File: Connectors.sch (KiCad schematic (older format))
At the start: 6 parts, among them J201 Conn_ARM_JTAG_SWD_10, J202 Conn_01x10, J203 Conn_01x04, J204 Conn_02x03_Counter_Clockwise

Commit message: updates to schematic
Signed-off-by: Thomas Schmid <tom@binary-kitchen.de>
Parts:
- J201: renamed from J202; footprint Connector_Molex:Molex_Micro-Latch_53254-1070_1x10_P2.00mm_Horizontal -> Connector_Molex:Molex_MicroClasp_55935-1010_1x10_P2.00mm_Horizontal
- J202: renamed from J201; footprint Connector_PinHeader_2.54mm:PinHeader_2x05_P2.54mm_Vertical -> Connector_PinHeader_2.00mm:PinHeader_2x05_P2.00mm_Vertical_SMD
- J203: renamed from J204; footprint Connector_PinHeader_2.54mm:PinHeader_2x03_P2.54mm_Horizontal -> Connector_PinHeader_2.00mm:PinHeader_2x05_P2.00mm_Vertical_SMD
- renumbered J203 to J204
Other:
- note added: "mosfets: Si7232DN"
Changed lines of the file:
@@
 $EndDescr
 $Comp
-L Connector:Conn_ARM_JTAG_SWD_10 J201
+L Connector:Conn_ARM_JTAG_SWD_10 J202
 U 1 1 5D3DE887
 P 2000 1500
-F 0 "J201" H 1557 1546 50  0000 R CNN
+F 0 "J202" H 1557 1546 50  0000 R CNN
 F 1 "Conn_ARM_JTAG_SWD_10" H 1557 1455 50  0000 R CNN
-F 2 "Connector_PinHeader_2.54mm:PinHeader_2x05_P2.54mm_Vertical" H 2000 1500 50  0001 C CNN
+F 2 "Connector_PinHeader_2.00mm:PinHeader_2x05_P2.00mm_Vertical_SMD" H 2000 1500 50  0001 C CNN
 F 3 "http://infocenter.arm.com/help/topic/com.arm.doc.ddi0314h/DDI0314H_coresight_components_trm.pdf" V 1650 250 50  0001 C CNN
 	1    2000 1500
@@
 ARM_L
 $Comp
-L Connector_Generic:Conn_01x10 J202
+L Connector_Generic:Conn_01x10 J201
 U 1 1 5D607587
 P 1600 3250
-F 0 "J202" H 1680 3242 50  0000 L CNN
+F 0 "J201" H 1680 3242 50  0000 L CNN
 F 1 "Conn_01x10" H 1680 3151 50  0000 L CNN
-F 2 "Connector_Molex:Molex_Micro-Latch_53254-1070_1x10_P2.00mm_Horizontal" H 1600 3250 50  0001 C CNN
+F 2 "Connector_Molex:Molex_MicroClasp_55935-1010_1x10_P2.00mm_Horizontal" H 1600 3250 50  0001 C CNN
 F 3 "~" H 1600 3250 50  0001 C CNN
 	1    1600 3250
@@
 $EndComp
 $Comp
-L Connector_Generic:Conn_01x04 J203
+L Connector_Generic:Conn_01x04 J204
 U 1 1 5D616D6A
 P 3250 2750
-F 0 "J203" H 3330 2742 50  0000 L CNN
+F 0 "J204" H 3330 2742 50  0000 L CNN
 F 1 "Conn_01x04" H 3330 2651 50  0000 L CNN
 F 2 "Connector_Molex:Molex_PicoBlade_53048-0410_1x04_P1.25mm_Horizontal" H 3250 2750 50  0001 C CNN
@@
 $EndComp
 $Comp
-L Connector_Generic:Conn_02x03_Counter_Clockwise J204
+L Connector_Generic:Conn_02x03_Counter_Clockwise J203
 U 1 1 5D61EC32
 P 3200 3500
-F 0 "J204" H 3250 3817 50  0000 C CNN
+F 0 "J203" H 3250 3817 50  0000 C CNN
 F 1 "Conn_02x03_Counter_Clockwise" H 3250 3726 50  0000 C CNN
-F 2 "Connector_PinHeader_2.54mm:PinHeader_2x03_P2.54mm_Horizontal" H 3200 3500 50  0001 C CNN
+F 2 "Connector_PinHeader_2.00mm:PinHeader_2x05_P2.00mm_Vertical_SMD" H 3200 3500 50  0001 C CNN
 F 3 "~" H 3200 3500 50  0001 C CNN
 	1    3200 3500
@@
 	1    0    0    -1
 $EndComp
+Text Notes 3100 1200 0    50   ~ 0
+mosfets: Si7232DN
 $EndSCHEMATC

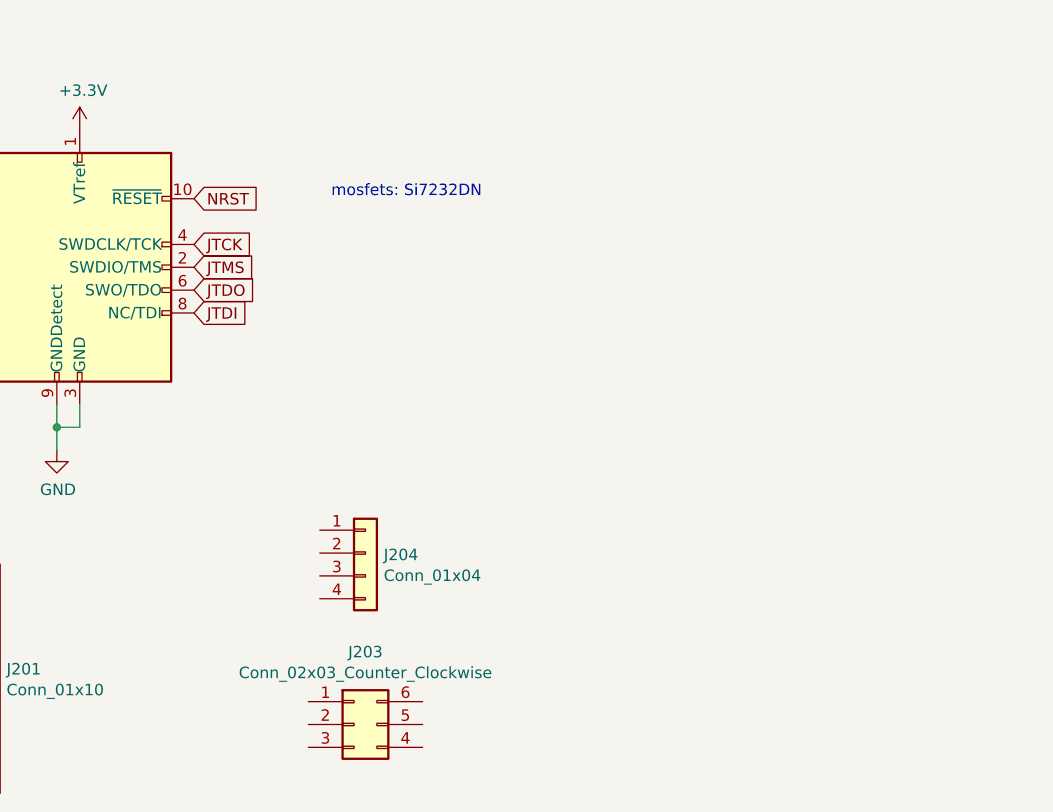
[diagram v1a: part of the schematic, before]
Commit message: add pyro output stages
Signed-off-by: Thomas Schmid <tom@binary-kitchen.de>
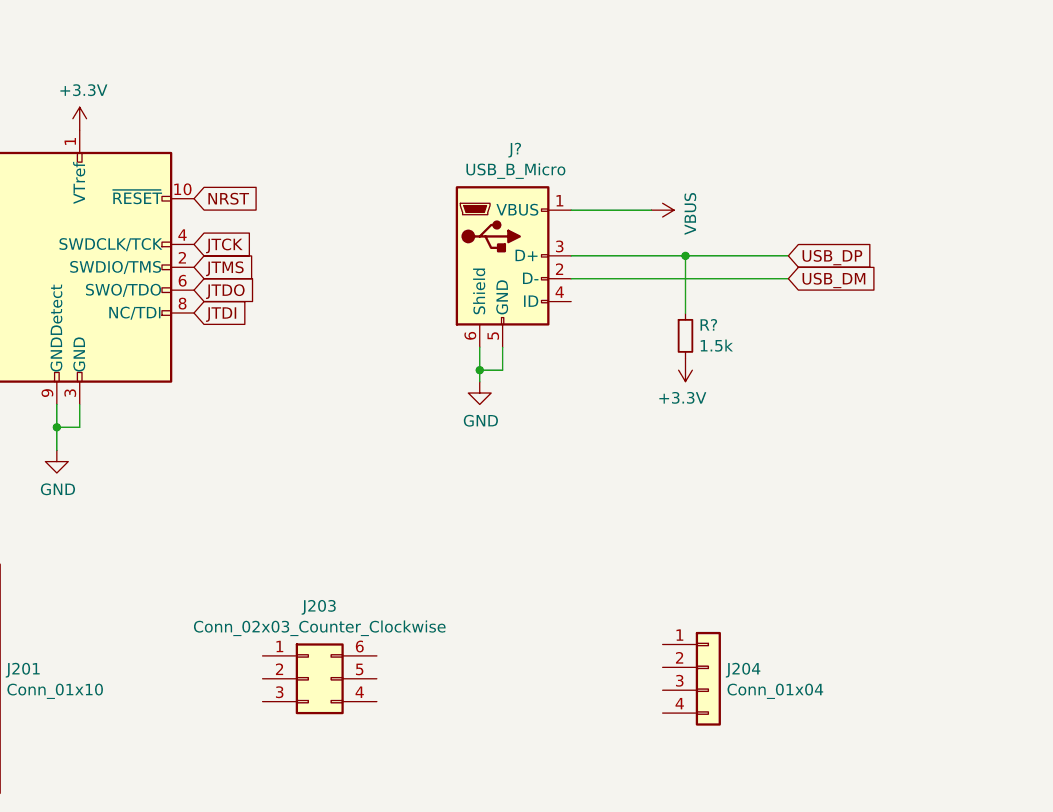
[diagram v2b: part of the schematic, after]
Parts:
- added J?: USB_B_Micro, Connector_USB:USB_Micro-B_Molex-105017-0001, symbol Connector:USB_B_Micro
- added R?: 1.5k, Resistor_SMD:R_0603_1608Metric_Pad1.05x0.95mm_HandSolder, symbol Device:R_Small
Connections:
- net labels added: USB_DM, USB_DP, VBUS
- wire segments 4 -> 13
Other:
- note removed: "mosfets: Si7232DN"
- moved on the sheet: J203, J204
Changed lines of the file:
@@
 $Descr A4 11693 8268
 encoding utf-8
-Sheet 2 2
+Sheet 2 5
 Title ""
 Date ""
@@
 L Connector_Generic:Conn_01x04 J204
 U 1 1 5D616D6A
-P 3250 2750
-F 0 "J204" H 3330 2742 50  0000 L CNN
-F 1 "Conn_01x04" H 3330 2651 50  0000 L CNN
-F 2 "Connector_Molex:Molex_PicoBlade_53048-0410_1x04_P1.25mm_Horizontal" H 3250 2750 50  0001 C CNN
-F 3 "~" H 3250 2750 50  0001 C CNN
-	1    3250 2750
+P 4750 3250
+F 0 "J204" H 4830 3242 50  0000 L CNN
+F 1 "Conn_01x04" H 4830 3151 50  0000 L CNN
+F 2 "Connector_Molex:Molex_PicoBlade_53048-0410_1x04_P1.25mm_Horizontal" H 4750 3250 50  0001 C CNN
+F 3 "~" H 4750 3250 50  0001 C CNN
+	1    4750 3250
 	1    0    0    -1
 $EndComp
@@
 L Connector_Generic:Conn_02x03_Counter_Clockwise J203
 U 1 1 5D61EC32
-P 3200 3500
-F 0 "J203" H 3250 3817 50  0000 C CNN
-F 1 "Conn_02x03_Counter_Clockwise" H 3250 3726 50  0000 C CNN
-F 2 "Connector_PinHeader_2.00mm:PinHeader_2x05_P2.00mm_Vertical_SMD" H 3200 3500 50  0001 C CNN
-F 3 "~" H 3200 3500 50  0001 C CNN
-	1    3200 3500
+P 3000 3300
+F 0 "J203" H 3050 3617 50  0000 C CNN
+F 1 "Conn_02x03_Counter_Clockwise" H 3050 3526 50  0000 C CNN
+F 2 "Connector_PinHeader_2.00mm:PinHeader_2x05_P2.00mm_Vertical_SMD" H 3000 3300 50  0001 C CNN
+F 3 "~" H 3000 3300 50  0001 C CNN
+	1    3000 3300
 	1    0    0    -1
 $EndComp
@@
 	1    0    0    -1
 $EndComp
-Text Notes 3100 1200 0    50   ~ 0
-mosfets: Si7232DN
+$Comp
+L Connector:USB_B_Micro J?
+U 1 1 5D5D0BB5
+P 3850 1450
+F 0 "J?" H 3907 1917 50  0000 C CNN
+F 1 "USB_B_Micro" H 3907 1826 50  0000 C CNN
+F 2 "Connector_USB:USB_Micro-B_Molex-105017-0001" H 4000 1400 50  0001 C CNN
+F 3 "~" H 4000 1400 50  0001 C CNN
+	1    3850 1450
+	1    0    0    -1
+$EndComp
+$Comp
+L power:GND #PWR?
+U 1 1 5D5D0BBB
+P 3750 2000
+F 0 "#PWR?" H 3750 1750 50  0001 C CNN
+F 1 "GND" H 3755 1827 50  0000 C CNN
+F 2 "" H 3750 2000 50  0001 C CNN
+F 3 "" H 3750 2000 50  0001 C CNN
+	1    3750 2000
+	1    0    0    -1
+$EndComp
+Wire Wire Line
+	3750 2000 3750 1950
+Wire Wire Line
+	3750 1950 3850 1950
+Wire Wire Line
+	3850 1950 3850 1850
+Connection ~ 3750 1950
+Wire Wire Line
+	3750 1950 3750 1850
+Wire Wire Line
+	4150 1250 4500 1250
+$Comp
+L power:VBUS #PWR?
+U 1 1 5D5D0BC7
+P 4500 1250
+F 0 "#PWR?" H 4500 1100 50  0001 C CNN
+F 1 "VBUS" H 4515 1423 50  0000 C CNN
+F 2 "" H 4500 1250 50  0001 C CNN
+F 3 "" H 4500 1250 50  0001 C CNN
+	1    4500 1250
+	0    1    1    0
+$EndComp
+Wire Wire Line
+	4650 1450 5100 1450
+Connection ~ 4650 1450
+Wire Wire Line
+	4650 1700 4650 1450
+$Comp
+L power:+3.3V #PWR?
+U 1 1 5D5D0BD0
+P 4650 1900
+F 0 "#PWR?" H 4650 1750 50  0001 C CNN
+F 1 "+3.3V" H 4665 2073 50  0000 C CNN
+F 2 "" H 4650 1900 50  0001 C CNN
+F 3 "" H 4650 1900 50  0001 C CNN
+	1    4650 1900
+	-1   0    0    1
+$EndComp
+$Comp
+L Device:R_Small R?
+U 1 1 5D5D0BD6
+P 4650 1800
+F 0 "R?" H 4709 1846 50  0000 L CNN
+F 1 "1.5k" H 4709 1755 50  0000 L CNN
+F 2 "Resistor_SMD:R_0603_1608Metric_Pad1.05x0.95mm_HandSolder" H 4650 1800 50  0001 C CNN
+F 3 "~" H 4650 1800 50  0001 C CNN
+	1    4650 1800
+	1    0    0    -1
+$EndComp
+Wire Wire Line
+	4150 1450 4650 1450
+Wire Wire Line
+	4150 1550 5100 1550
+Text GLabel 5100 1450 2    50   Input ~ 0
+USB_DP
+Text GLabel 5100 1550 2    50   Input ~ 0
+USB_DM
 $EndSCHEMATC

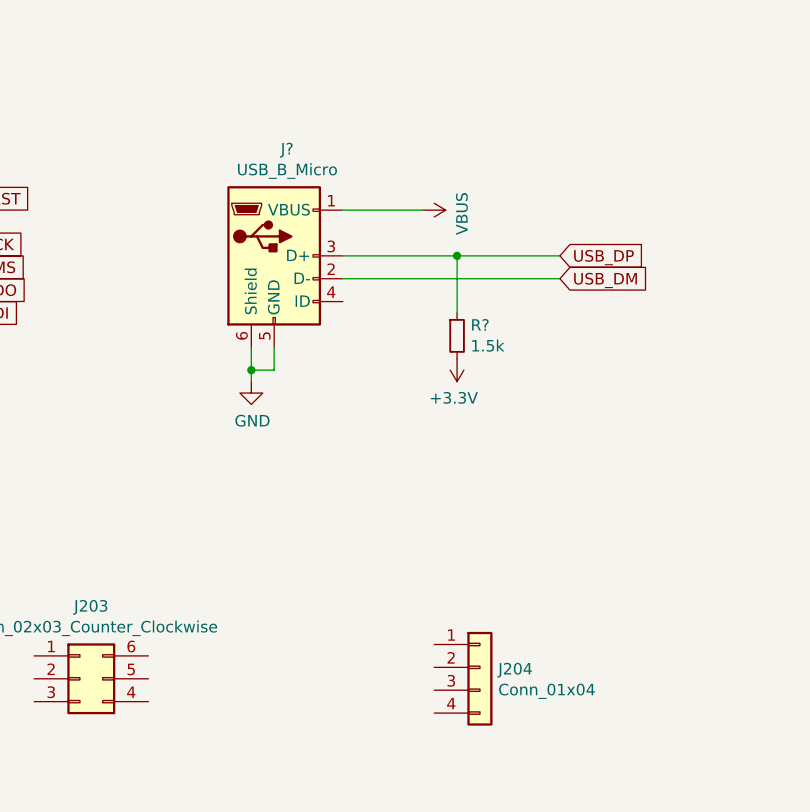
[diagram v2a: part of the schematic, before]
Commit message: update pyro output stage. add a fuse to the test circuit and remove pullup for sense line
Signed-off-by: Thomas Schmid <tom@binary-kitchen.de>
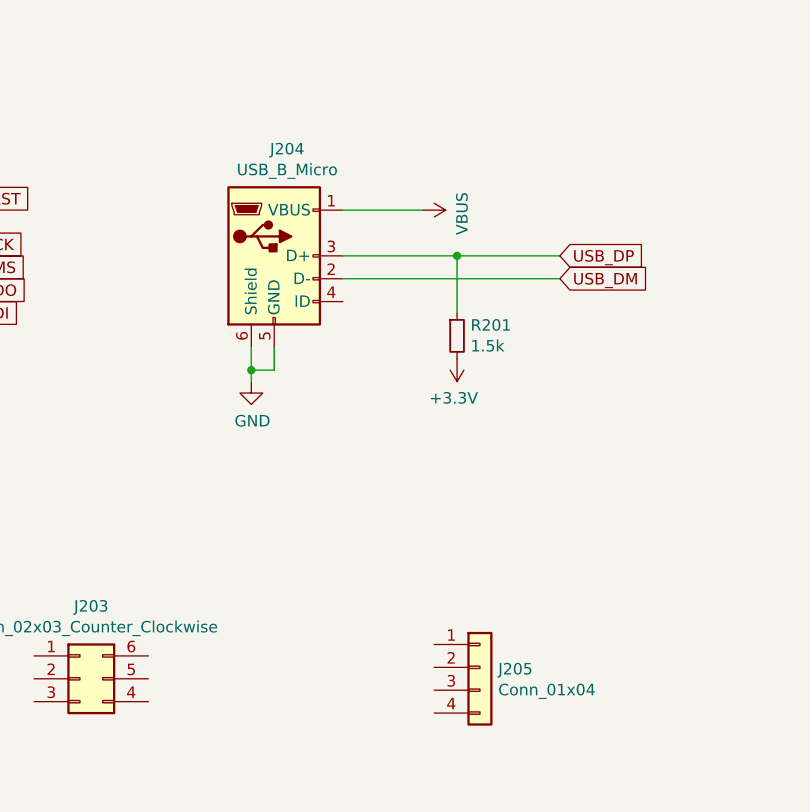
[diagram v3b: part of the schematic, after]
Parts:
- R201: renamed from R?; footprint Resistor_SMD:R_0603_1608Metric_Pad1.05x0.95mm_HandSolder -> Resistor_SMD:R_0402_1005Metric
- gave numbers to parts that had none: 1
- renumbered J204 to J205
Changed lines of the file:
@@
 JTDO
 $Comp
-L power:+3.3V #PWR0106
+L power:+3.3V #PWR0204
 U 1 1 5D3E0632
 P 2000 900
-F 0 "#PWR0106" H 2000 750 50  0001 C CNN
+F 0 "#PWR0204" H 2000 750 50  0001 C CNN
 F 1 "+3.3V" H 2015 1073 50  0000 C CNN
 F 2 "" H 2000 900 50  0001 C CNN
@@
 $EndComp
 $Comp
-L power:GND #PWR0107
+L power:GND #PWR0203
 U 1 1 5D3E119D
 P 1900 2300
-F 0 "#PWR0107" H 1900 2050 50  0001 C CNN
+F 0 "#PWR0203" H 1900 2050 50  0001 C CNN
 F 1 "GND" H 1905 2127 50  0000 C CNN
 F 2 "" H 1900 2300 50  0001 C CNN
@@
 $EndComp
 $Comp
-L power:+BATT #PWR0134
+L power:+BATT #PWR0201
 U 1 1 5D607F65
 P 1400 2850
-F 0 "#PWR0134" H 1400 2700 50  0001 C CNN
+F 0 "#PWR0201" H 1400 2700 50  0001 C CNN
 F 1 "+BATT" V 1415 2977 50  0000 L CNN
 F 2 "" H 1400 2850 50  0001 C CNN
@@
 $EndComp
 $Comp
-L power:GND #PWR0135
+L power:GND #PWR0202
 U 1 1 5D60861A
 P 1400 2950
-F 0 "#PWR0135" H 1400 2700 50  0001 C CNN
+F 0 "#PWR0202" H 1400 2700 50  0001 C CNN
 F 1 "GND" V 1405 2822 50  0000 R CNN
 F 2 "" H 1400 2950 50  0001 C CNN
@@
 $EndComp
 $Comp
-L Connector_Generic:Conn_01x04 J204
+L Connector_Generic:Conn_01x04 J205
 U 1 1 5D616D6A
 P 4750 3250
-F 0 "J204" H 4830 3242 50  0000 L CNN
+F 0 "J205" H 4830 3242 50  0000 L CNN
 F 1 "Conn_01x04" H 4830 3151 50  0000 L CNN
 F 2 "Connector_Molex:Molex_PicoBlade_53048-0410_1x04_P1.25mm_Horizontal" H 4750 3250 50  0001 C CNN
@@
 $EndComp
 $Comp
-L Connector:USB_B_Micro J?
+L Connector:USB_B_Micro J204
 U 1 1 5D5D0BB5
 P 3850 1450
-F 0 "J?" H 3907 1917 50  0000 C CNN
+F 0 "J204" H 3907 1917 50  0000 C CNN
 F 1 "USB_B_Micro" H 3907 1826 50  0000 C CNN
 F 2 "Connector_USB:USB_Micro-B_Molex-105017-0001" H 4000 1400 50  0001 C CNN
@@
 $EndComp
 $Comp
-L power:GND #PWR?
+L power:GND #PWR0205
 U 1 1 5D5D0BBB
 P 3750 2000
-F 0 "#PWR?" H 3750 1750 50  0001 C CNN
+F 0 "#PWR0205" H 3750 1750 50  0001 C CNN
 F 1 "GND" H 3755 1827 50  0000 C CNN
 F 2 "" H 3750 2000 50  0001 C CNN
@@
 	4150 1250 4500 1250
 $Comp
-L power:VBUS #PWR?
+L power:VBUS #PWR0206
 U 1 1 5D5D0BC7
 P 4500 1250
-F 0 "#PWR?" H 4500 1100 50  0001 C CNN
+F 0 "#PWR0206" H 4500 1100 50  0001 C CNN
 F 1 "VBUS" H 4515 1423 50  0000 C CNN
 F 2 "" H 4500 1250 50  0001 C CNN
@@
 	4650 1700 4650 1450
 $Comp
-L power:+3.3V #PWR?
+L power:+3.3V #PWR0207
 U 1 1 5D5D0BD0
 P 4650 1900
-F 0 "#PWR?" H 4650 1750 50  0001 C CNN
+F 0 "#PWR0207" H 4650 1750 50  0001 C CNN
 F 1 "+3.3V" H 4665 2073 50  0000 C CNN
 F 2 "" H 4650 1900 50  0001 C CNN
@@
 $EndComp
 $Comp
-L Device:R_Small R?
+L Device:R_Small R201
 U 1 1 5D5D0BD6
 P 4650 1800
-F 0 "R?" H 4709 1846 50  0000 L CNN
+F 0 "R201" H 4709 1846 50  0000 L CNN
 F 1 "1.5k" H 4709 1755 50  0000 L CNN
-F 2 "Resistor_SMD:R_0603_1608Metric_Pad1.05x0.95mm_HandSolder" H 4650 1800 50  0001 C CNN
+F 2 "Resistor_SMD:R_0402_1005Metric" H 4650 1800 50  0001 C CNN
 F 3 "~" H 4650 1800 50  0001 C CNN
 	1    4650 1800

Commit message: more work on schematic and layout
Signed-off-by: Thomas Schmid <tom@lfence.de>
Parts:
- H201, H202: footprint MountingHole:MountingHole_3.2mm_M3_DIN965 -> MountingHole:MountingHole_3.2mm_M3_Pad_Via
- J203: footprint Connector_PinHeader_2.00mm:PinHeader_2x05_P2.00mm_Vertical_SMD -> Connector_PinHeader_2.54mm:PinHeader_2x03_P2.54mm_Horizontal
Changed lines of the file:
@@
 F 0 "J203" H 3050 3617 50  0000 C CNN
 F 1 "Conn_02x03_Counter_Clockwise" H 3050 3526 50  0000 C CNN
-F 2 "Connector_PinHeader_2.00mm:PinHeader_2x05_P2.00mm_Vertical_SMD" H 3000 3300 50  0001 C CNN
+F 2 "Connector_PinHeader_2.54mm:PinHeader_2x03_P2.54mm_Horizontal" H 3000 3300 50  0001 C CNN
 F 3 "~" H 3000 3300 50  0001 C CNN
 	1    3000 3300
@@
 U 1 1 5D62934E
 P 8350 1000
+AR Path="/5D3DE309/5D62934E" Ref="H201"  Part="1"
+AR Path="/5D62934E" Ref="H201"  Part="1"
 F 0 "H201" H 8450 1046 50  0000 L CNN
 F 1 "MountingHole" H 8450 955 50  0000 L CNN
-F 2 "MountingHole:MountingHole_3.2mm_M3_DIN965" H 8350 1000 50  0001 C CNN
+F 2 "MountingHole:MountingHole_3.2mm_M3_Pad_Via" H 8350 1000 50  0001 C CNN
 F 3 "~" H 8350 1000 50  0001 C CNN
 	1    8350 1000
@@
 F 0 "H202" H 8450 1296 50  0000 L CNN
 F 1 "MountingHole" H 8450 1205 50  0000 L CNN
-F 2 "MountingHole:MountingHole_3.2mm_M3_DIN965" H 8350 1250 50  0001 C CNN
+F 2 "MountingHole:MountingHole_3.2mm_M3_Pad_Via" H 8350 1250 50  0001 C CNN
 F 3 "~" H 8350 1250 50  0001 C CNN
 	1    8350 1250

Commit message: update to schematic and layout
Signed-off-by: Thomas Schmid <tom@lfence.de>
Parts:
- H201, H202: symbol Mechanical:MountingHole -> Mechanical:MountingHole_Pad
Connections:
- net labels added: PYRO0_HIGH, PYRO0_LOW
- net labels removed: ARM_H, ARM_L
- wire segments 13 -> 17
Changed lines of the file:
@@
 $Descr A4 11693 8268
 encoding utf-8
-Sheet 2 5
+Sheet 2 6
 Title ""
 Date ""
@@
 Text GLabel 1400 3650 0    50   Input ~ 0
 PYRO3_HIGH
-Text GLabel 1400 3050 0    50   Input ~ 0
-ARM_H
-Text GLabel 1400 3150 0    50   Input ~ 0
-ARM_L
 $Comp
 L Connector_Generic:Conn_01x10 J201
@@
 $EndComp
 $Comp
-L Mechanical:MountingHole H201
+L Mechanical:MountingHole_Pad H201
 U 1 1 5D62934E
 P 8350 1000
@@
 $EndComp
 $Comp
-L Mechanical:MountingHole H202
+L Mechanical:MountingHole_Pad H202
 U 1 1 5D62B183
-P 8350 1250
-F 0 "H202" H 8450 1296 50  0000 L CNN
-F 1 "MountingHole" H 8450 1205 50  0000 L CNN
-F 2 "MountingHole:MountingHole_3.2mm_M3_Pad_Via" H 8350 1250 50  0001 C CNN
-F 3 "~" H 8350 1250 50  0001 C CNN
-	1    8350 1250
+P 9150 1000
+F 0 "H202" H 9250 1046 50  0000 L CNN
+F 1 "MountingHole" H 9250 955 50  0000 L CNN
+F 2 "MountingHole:MountingHole_3.2mm_M3_Pad_Via" H 9150 1000 50  0001 C CNN
+F 3 "~" H 9150 1000 50  0001 C CNN
+	1    9150 1000
 	1    0    0    -1
 $EndComp
@@
 Text GLabel 5100 1550 2    50   Input ~ 0
 USB_DM
+Text GLabel 1400 3050 0    50   Input ~ 0
+PYRO0_HIGH
+Text GLabel 1400 3150 0    50   Input ~ 0
+PYRO0_LOW
+Wire Wire Line
+	8350 1100 8350 1250
+Wire Wire Line
+	8350 1250 9150 1250
+Wire Wire Line
+	9150 1250 9150 1100
+$Comp
+L power:GND #PWR0138
+U 1 1 5D53B2A1
+P 8350 1400
+F 0 "#PWR0138" H 8350 1150 50  0001 C CNN
+F 1 "GND" H 8355 1227 50  0000 C CNN
+F 2 "" H 8350 1400 50  0001 C CNN
+F 3 "" H 8350 1400 50  0001 C CNN
+	1    8350 1400
+	1    0    0    -1
+$EndComp
+Wire Wire Line
+	8350 1400 8350 1250
+Connection ~ 8350 1250
 $EndSCHEMATC

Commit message: more work on schematic and layout
Signed-off-by: Thomas Schmid <tom@binary-kitchen.de>
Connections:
- net JTDI: no longer names the net of J202.8 (NC/TDI)
- net USB_DM renamed USB_D_N
- net USB_DP renamed USB_D_P
- no-connect marks 0 -> 1
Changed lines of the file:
@@
 Wire Wire Line
 	1900 2200 1900 2100
-Text GLabel 2500 1700 2    50   Input ~ 0
-JTDI
 Text GLabel 1400 3550 0    50   Input ~ 0
 PYRO2_LOW
@@
 	4150 1550 5100 1550
 Text GLabel 5100 1450 2    50   Input ~ 0
-USB_DP
+USB_D_P
 Text GLabel 5100 1550 2    50   Input ~ 0
-USB_DM
+USB_D_N
 Text GLabel 1400 3050 0    50   Input ~ 0
 PYRO0_HIGH
@@
 	8350 1400 8350 1250
 Connection ~ 8350 1250
+NoConn ~ 2500 1700
 $EndSCHEMATC

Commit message: major work on layout. nearly finished
Signed-off-by: Thomas Schmid <tom@binary-kitchen.de>
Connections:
- net JTCK renamed SWCLK
- net JTDO renamed SWO
- net JTMS renamed SWDIO
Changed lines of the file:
@@
 NRST
 Text GLabel 2500 1400 2    50   Input ~ 0
-JTCK
+SWCLK
 Text GLabel 2500 1500 2    50   Input ~ 0
-JTMS
+SWDIO
 Text GLabel 2500 1600 2    50   Input ~ 0
-JTDO
+SWO
 $Comp
 L power:+3.3V #PWR0204
